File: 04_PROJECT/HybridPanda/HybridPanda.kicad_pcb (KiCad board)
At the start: 4 copper layers, 50.5 x 46.7 mm, 120 parts, among them J1 SWD, P1 TYPE-C-31-M-04, Q1 DDTA143ECA-7-F P08, Q2 DDTA143ECA-7-F P08, Q3 PDTC114EU, Q4 HY12P03C2, SW1 SW_Push, U1 AP22615AWU-7, U10 TJA1042TK-3, U11 TJA1042TK-3, U12 XL1509-3.3, U3 10_0_QHHTZB6_3, U5 FM-B1921RGBA-SH, U6 TPS5450DDAR, U7 STM32H725ZGT6, U8 TJA1042TK-3, U9 TJA1042TK-3, Y1 25MHz X322525MOB4SI

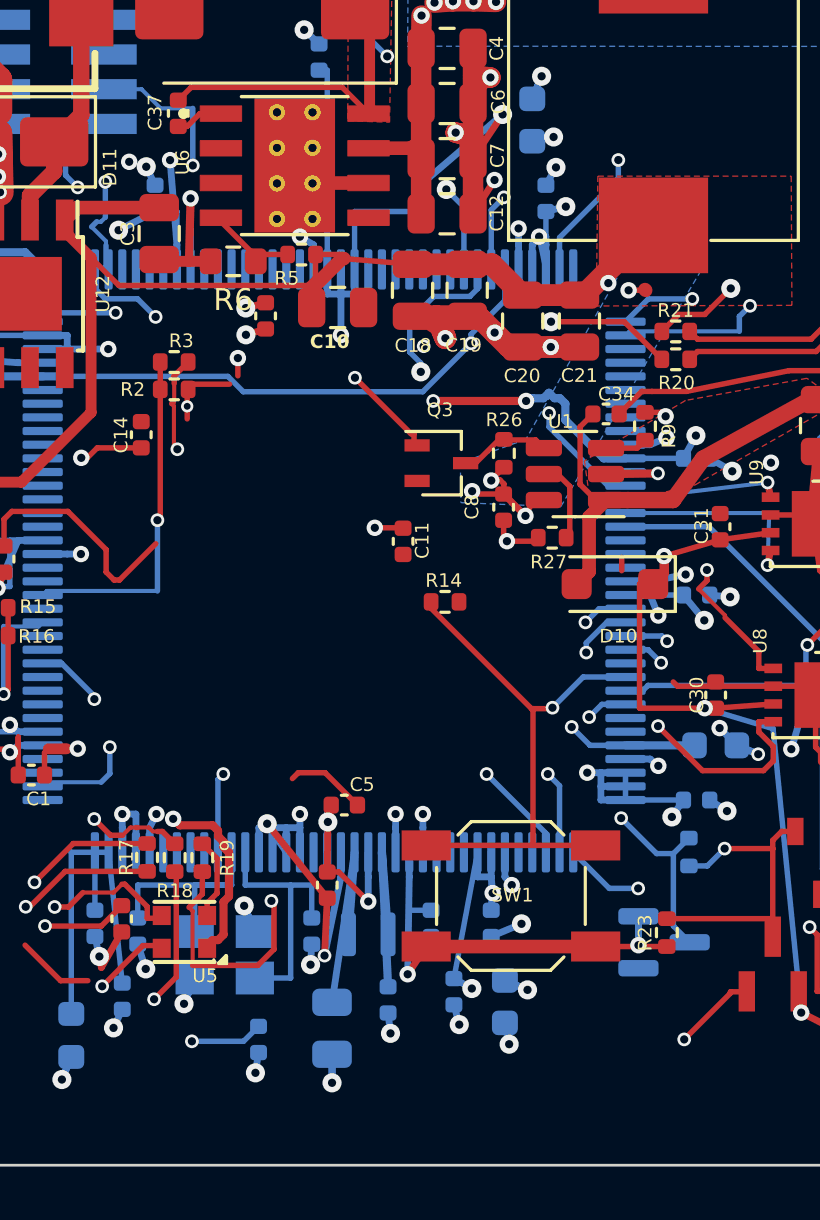
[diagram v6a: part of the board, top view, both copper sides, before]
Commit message: Step 2: PCR-2 VFBSMPS-VCAP link, C64/C65 decoupling, PCR-1 PF9 solder jumper
Schematic: VFBSMPS global labels renamed to VCAP (ST AN5419 direct-SMPS
topology, VFBSMPS tied to VCAP; L5 2.2uH + C41/C42 kept on VLXSMPS/VCAP).
Added C64 2.2uF 0402 at VCAP pin 103, C65 4.7uF 0603 at VDDSMPS pin 16.
PCR-1: PF9 (HW_TYPE id1 bit 2) lifted from the GND strap and wired to JP1
(SolderJumper_2_Open, net Net-(JP1-B)); JP1 closed = RED (id1=0), open =
HYBRID (id1=4). ERC 0 errors.

PCB (05_SCRIPTS/corr_step2_pcb.py): net merge, PF7/PF8/PF10 GND straps
rebuilt, PF9 via + F.Cu track to JP1 (F.Cu 107.6,72.9), C65 on F.Cu
(109.3,70.1) 2.5 mm from pin 16, C64 on B.Cu (116.28,44.0) 1.5 mm from
pad 103 (SWDIO via moved 0.15 mm, C54 slid 0.15 mm east, pad 104 stub via
removed - pad stays on the B.Cu GND zone), VCAP link C42.1 -> via
(110.725,72.752) -> In1 13.9 mm -> existing VCAP In1 copper, 0.3 mm wide.
parity profile: PF9 expect float_or_low (JP1 strap).

Gates: DRC 0 clearance / 0 unconnected, 184 total (starved_thermal 17->18:
U7 pad 104), step7_validate no failures, final_audit shorts 0 / vip 0, ERC
0 errors.

Co-authored-by: Copilot <223556219+Copilot@users.noreply.github.com>
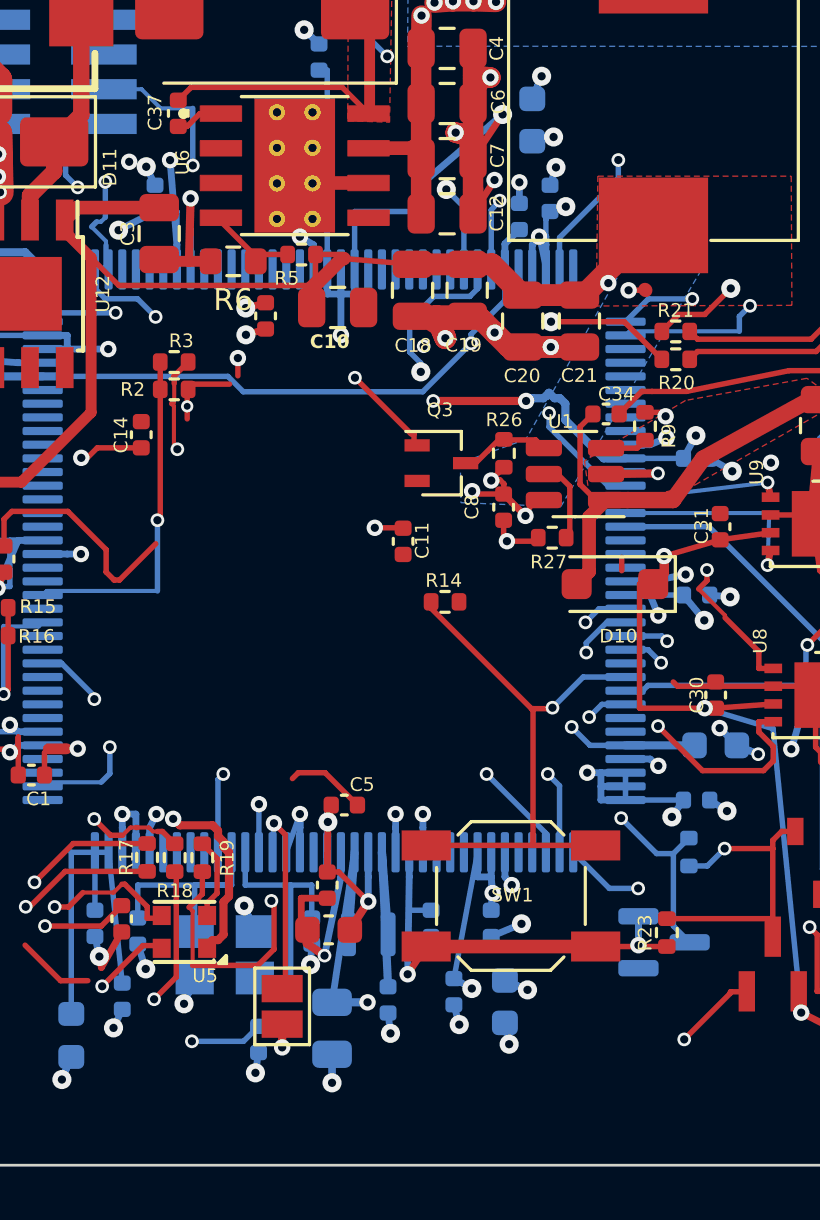
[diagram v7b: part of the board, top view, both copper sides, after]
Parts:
- added C64: 2.2uF, Capacitor_SMD:C_0402_1005Metric, B.Cu at (116.3, 44.0)
- added C65: 4.7uF, Capacitor_SMD:C_0603_1608Metric, F.Cu at (109.3, 70.1)
- added JP1: HW_ID1, Jumper:SolderJumper-2_P1.3mm_Open_Pad1.0x1.5mm, F.Cu at (107.6, 72.9)
- moved C54 0.15 mm to (117.4, 43.3)
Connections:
- C42 pad 1: VFBSMPS -> VCAP
- L5 pad 2: VFBSMPS -> VCAP
- U7 pad 17: VFBSMPS -> VCAP
- U7 pad 23: GND -> Net-(JP1-B)
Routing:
- net VCAP: track 43.6 -> 69.0 mm, vias 2 -> 3
- net VFBSMPS: track 8.56 -> 0.00 mm
- net Net-(JP1-B): track 0.00 -> 7.41 mm, vias 0 -> 1
- net GND: track 227.0 -> 223.3 mm, vias 73 -> 74
- net +3V3: track 318.9 -> 320.0 mm
